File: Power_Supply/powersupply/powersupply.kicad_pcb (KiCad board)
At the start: 2 copper layers, 70.9 x 74.5 mm, 66 parts, among them J1 Conn_01x03, J2 USB_B_Micro, Q1 Q_PMOS_GDS, SW1 SW_Push, U1 AZ1117E-3.3, U10 MCP6001-OT, U2 ATSAMD10D13A-SS, U3 B0505S-2WR2, U4 TFT_OLED, U5 joystick-K1-1506DN-01, U6 MC33063AP1, U7 LM358P, U8 1x2, U9 1x2

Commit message: new layout
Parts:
- R11: renamed from R13; value 0.05 -> 0.1
- moved C2 1.33 mm to (68.3, 64.1)
- moved R1 0.44 mm to (66.5, 32.0)
- moved U3 0.35 mm to (53.2, 40.0)
- moved R104 0.34 mm to (89.0, 26.6)
- moved R105 0.28 mm to (86.0, 26.6)
- moved TP2 0.28 mm to (79.7, 51.4)
- moved L1 0.22 mm to (70.8, 77.3)
- renumbered R14 to R1, R9 to R10, R17 to R12, R6 to R13, R7 to R14, R10 to R15, R12 to R16, R11 to R17, R3 to R2, R2 to R3, R16 to R4, R15 to R5, R1 to R6, R4 to R7, R5 to R8, R8 to R9
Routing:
- net /SDA: track 18.1 -> 16.0 mm
- net /SCK: track 25.6 -> 24.2 mm
- net GND: track 44.3 -> 45.4 mm
- net Net-(C2-Pad1): track 5.84 -> 6.50 mm
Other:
- board size 70.9 x 74.5 mm -> 70.9 x 74.4 mm

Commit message: finalish changes
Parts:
- SW1: value SW_Push -> KMR2; footprint Button_Switch_THT:SW_PUSH_6mm -> Button_Switch_SMD:SW_Push_1P1T_NO_CK_KMR2
- TP10, TP11, TP8, TP9: footprint TestPoint:TestPoint_Pad_1.5x1.5mm -> powersupply:pads
- moved TP5 10.4 mm to (99.8, 73.6)
- moved SW1 3.61 mm to (112.6, 32.7), turned to 90 degrees
- moved TP8 3.58 mm to (76.4, 26.2)
- moved Q1 3.17 mm to (94.6, 74.7)
- moved TP10 2.91 mm to (79.8, 26.2)
- moved D2 2.83 mm to (90.0, 78.5)
- moved TP11 2.11 mm to (81.3, 26.2)
- moved TP9 1.89 mm to (77.8, 26.2)
- moved R11 1.84 mm to (89.4, 67.2)
- moved TP6 1.41 mm to (66.5, 47.1)
- moved R10 1.26 mm to (99.5, 63.4)
- moved R9 0.76 mm to (89.4, 59.8)
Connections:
- SW1 pad 1: Net-(R101-Pad2) -> GND
- SW1 pad 2: GND -> Net-(R101-Pad2)
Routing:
- net /Voltage_limit_divider: track 31.5 -> 41.1 mm
- net GND: track 45.4 -> 49.1 mm, vias 6 -> 8
- net Net-(R101-Pad2): track 48.0 -> 44.4 mm
- net /V_negative_out: track 61.8 -> 58.4 mm
- net /Boost_out: track 79.0 -> 76.8 mm
- net Net-(R10-Pad1): track 39.4 -> 37.6 mm
- net +3V3: track 121.5 -> 122.5 mm
- net /V_current_amplified: track 24.5 -> 25.3 mm
- net /V_boost_ctrl: track 69.5 -> 68.7 mm
- net Net-(D2-Pad1): track 15.6 -> 14.9 mm
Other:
- outline, holes or cut-outs redrawn
- board text removed: "- +"

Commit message: big CHANGES
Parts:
- removed R12, R5: 10k, Resistor_THT:R_Axial_DIN0207_L6.3mm_D2.5mm_P10.16mm_Horizontal
- removed R4: 100, Resistor_THT:R_Axial_DIN0207_L6.3mm_D2.5mm_P10.16mm_Horizontal
- added C6: .1uF, Capacitor_THT:C_Rect_L4.0mm_W2.5mm_P2.50mm, F.Cu at (92.6, 4.60)
- added D4: C503B 2.1V, LED_THT:LED_D3.0mm_Horizontal_O1.27mm_Z6.0mm, F.Cu at (86.8, 4.35)
- added R18: 300, Resistor_SMD:R_0805_2012Metric, F.Cu at (93.2, 8.10)
- added R19: 18.2k, Resistor_SMD:R_0805_2012Metric, F.Cu at (98.9, 4.05)
- added R20: 4.99k, Resistor_SMD:R_0805_2012Metric, F.Cu at (93.2, 11.1)
- C3: value 470u -> 470uF; footprint Capacitor_THT:CP_Radial_D10.0mm_P5.00mm -> Capacitor_THT:CP_Radial_D8.0mm_P3.50mm
- C4: value 470u -> 100uF; footprint Capacitor_THT:CP_Radial_D10.0mm_P5.00mm -> Capacitor_THT:CP_Radial_D6.3mm_P2.50mm
- C5: footprint Capacitor_THT:CP_Radial_D10.0mm_P5.00mm -> Capacitor_THT:CP_Radial_D6.3mm_P2.50mm
- D101: renamed from D3; footprint Diode_THT:D_DO-201AE_P15.24mm_Horizontal -> Diode_SMD:D_SOD-323
- J3: renamed from U9; footprint Connector_PinHeader_2.54mm:PinHeader_1x02_P2.54mm_Vertical -> Connector_PinHeader_2.54mm:PinHeader_1x02_P2.54mm_Horizontal
- L2: footprint Inductor_THT:L_Axial_L11.0mm_D4.5mm_P15.24mm_Horizontal_Fastron_MECC -> powersupply:11R102C_Inductor
- R1: value 1k -> 150
- R10, R13, R14, R15, R16, R17, R3, R6, R7, R8: footprint Resistor_THT:R_Axial_DIN0207_L6.3mm_D2.5mm_P10.16mm_Horizontal -> Resistor_SMD:R_0805_2012Metric
- R9: value 10k -> 130k; footprint Resistor_THT:R_Axial_DIN0207_L6.3mm_D2.5mm_P10.16mm_Horizontal -> Resistor_SMD:R_0805_2012Metric
- TP10: value TestPoint -> pin_2_pad
- TP11: value TestPoint -> pin_2_alt
- TP8: value TestPoint -> pin_1_alt
- TP9: value TestPoint -> pin_1_pad
- U10: value MCP6001-OT -> INA199; footprint Package_TO_SOT_SMD:SOT-23-5 -> Package_TO_SOT_SMD:SOT-363_SC-70-6
- U6: footprint Package_SO:SOIC-8_3.9x4.9mm_P1.27mm -> Package_DIP:DIP-8_W7.62mm
- moved TP4 109.9 mm to (2.20, 103.4)
- moved TP3 105.0 mm to (-0.90, 87.7)
- moved TP5 89.9 mm to (12.7, 95.9)
- moved TP6 70.6 mm to (2.30, 76.3)
- moved TP1 67.9 mm to (13.9, 81.5)
- moved TP7 47.7 mm to (13.8, 110.9)
- moved U10 47.4 mm to (97.6, 8.55), turned to 0 degrees
- moved L1 27.2 mm to (43.8, 80.8)
- moved J3 26.8 mm to (78.2, 87.7)
- moved R3 22.0 mm to (42.5, 72.9), turned to 90 degrees
- moved R2 20.4 mm to (39.2, 79.0)
- moved L2 20.4 mm to (33.4, 68.1)
- moved U3 17.9 mm to (36.0, 44.9)
- moved D101 17.4 mm to (46.5, 37.7)
- moved C105 17.3 mm to (54.8, 39.3)
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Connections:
- C105 pad 1: /V_boost_ctrl -> /V_lin_ctrl
- R103 pad 1: /V_boost_ctrl -> /V_lin_ctrl
- U10 pad 1: /V_current_amplified -> GND
- U10 pad 3: Net-(R10-Pad1) -> +3V3
- U10 pad 4: Net-(R4-Pad1) -> /V_negative_out
- U10 pad 5: +3V3 -> GND
- U2 pad 18: /V_lin_ctrl -> /V_boost_ctrl
- U2 pad 8: /V_positive_out -> Net-(R19-Pad2)
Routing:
- net /V_positive_out: track 151.8 -> 0.00 mm
- net +3V3: track 122.5 -> 0.00 mm
- net +5V: track 81.1 -> 0.00 mm, vias 2 -> 0
- net /Boost_out: track 76.8 -> 0.00 mm
- net /V_boost_ctrl: track 68.7 -> 0.00 mm
- net Net-(C3-Pad1): track 62.7 -> 0.00 mm
- net /V_lin_ctrl: track 61.2 -> 0.00 mm
- net /V_negative_out: track 58.4 -> 0.00 mm, vias 2 -> 0
- net /V_curr_lim: track 57.8 -> 0.00 mm, vias 2 -> 0
- net GND: track 49.1 -> 0.00 mm, vias 8 -> 1
- net Net-(R101-Pad2): track 44.4 -> 0.00 mm, vias 2 -> 0
- net /Voltage_limit_divider: track 41.1 -> 0.00 mm
- net Net-(R10-Pad1): track 37.6 -> 0.00 mm
- net /Current_limit_divider: track 30.4 -> 0.00 mm
- net Net-(D2-Pad2): track 29.0 -> 0.00 mm
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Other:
- outline, holes or cut-outs redrawn

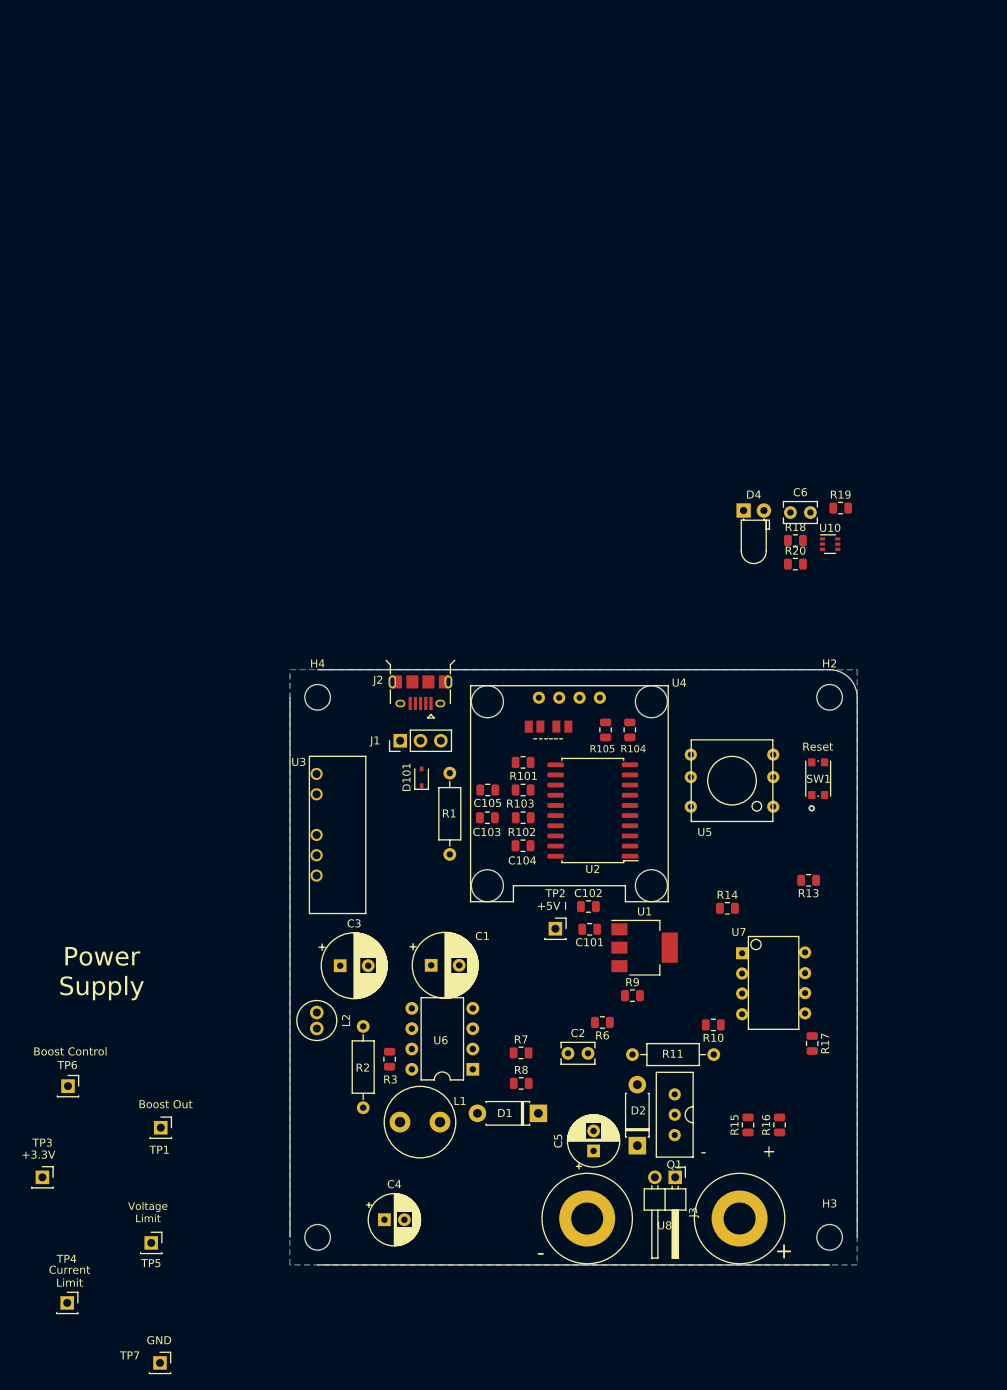
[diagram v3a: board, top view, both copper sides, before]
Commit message: new layout for power supply
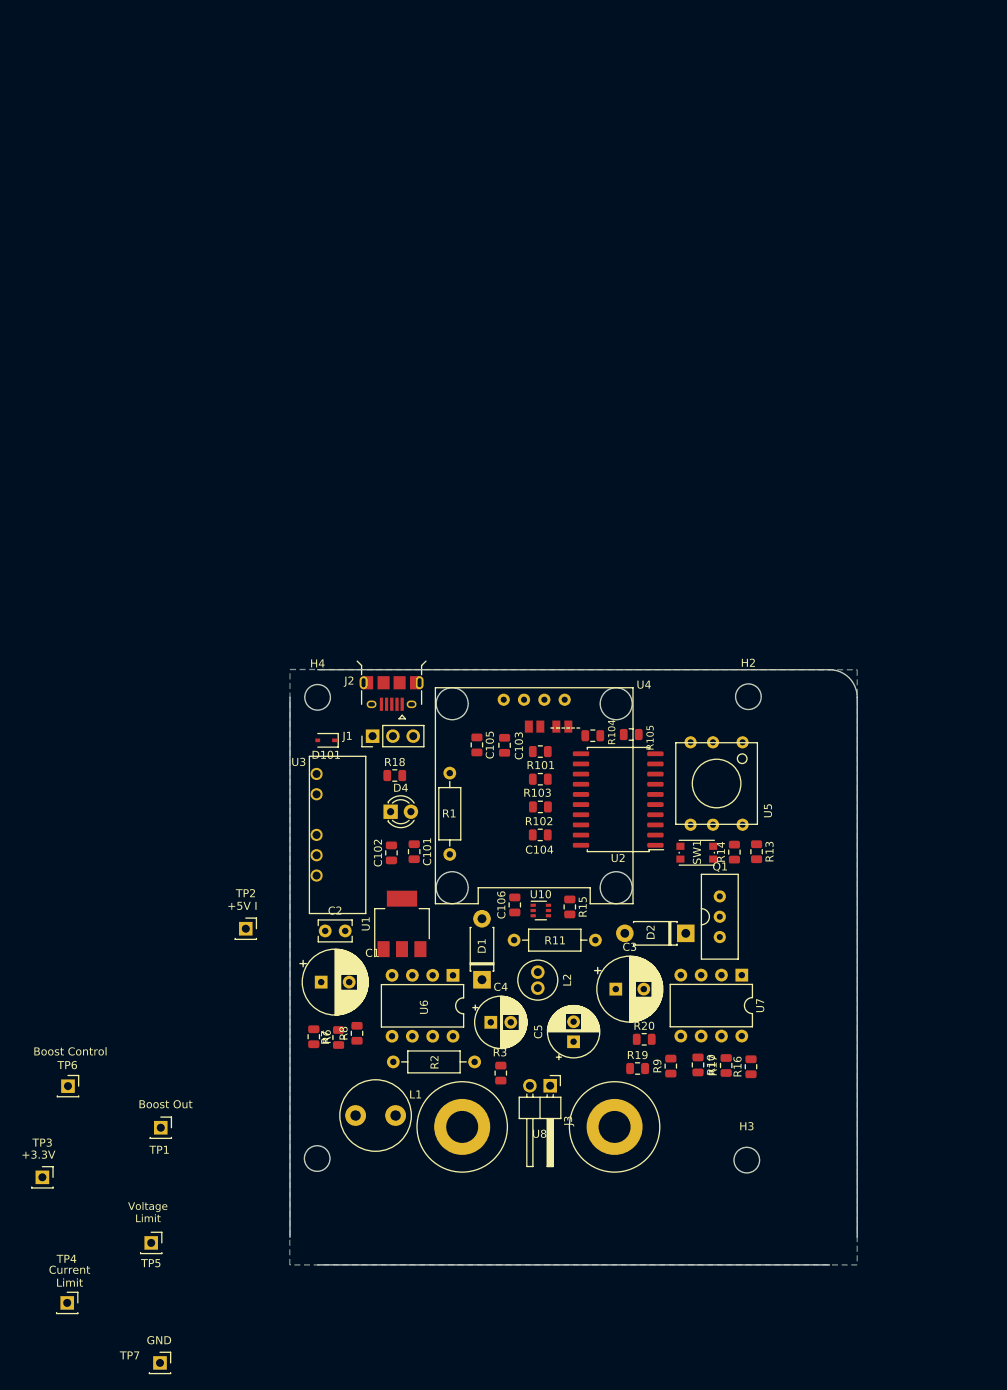
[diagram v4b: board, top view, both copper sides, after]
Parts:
- removed C6: .1uF, Capacitor_THT:C_Rect_L4.0mm_W2.5mm_P2.50mm
- added C106: .1uF, Capacitor_SMD:C_0805_2012Metric, F.Cu at (58.1, 53.6)
- D4: footprint LED_THT:LED_D3.0mm_Horizontal_O1.27mm_Z6.0mm -> LED_THT:LED_D3.0mm
- U7: footprint powersupply:LM358P -> Package_DIP:DIP-8_W7.62mm
- moved R19 74.5 mm to (73.5, 74.1)
- moved R20 62.3 mm to (74.3, 70.5)
- moved U10 58.4 mm to (61.4, 54.4)
- moved R18 58.1 mm to (43.1, 37.5)
- moved D4 58.0 mm to (42.6, 42.0)
- moved TP2 38.7 mm to (24.5, 56.6)
- moved R6 36.1 mm to (33.0, 70.1), turned to 270 degrees
- moved R15 35.2 mm to (65.0, 53.9), turned to 270 degrees
- moved C3 34.6 mm to (70.8, 64.2)
- moved C2 34.0 mm to (34.5, 56.9)
- moved U1 30.5 mm to (44.0, 56.0), turned to 90 degrees
- moved L2 28.1 mm to (61.0, 63.0)
- moved C4 28.0 mm to (55.1, 68.3)
- moved D2 27.2 mm to (79.5, 57.2), turned to 180 degrees
- moved C102 25.5 mm to (42.7, 47.1), turned to 90 degrees
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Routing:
- net GND: vias 1 -> 0
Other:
- board text removed: "+"
- board text removed: "-"
- board text removed: "Power Supply"
- board text removed: "Reset"

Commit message: big CHANGES
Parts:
- R1: footprint Resistor_THT:R_Axial_DIN0207_L6.3mm_D2.5mm_P10.16mm_Horizontal -> Resistor_SMD:R_0805_2012Metric
- R18: footprint Resistor_SMD:R_0805_2012Metric -> Resistor_THT:R_Axial_DIN0207_L6.3mm_D2.5mm_P10.16mm_Horizontal
- moved SW1 40.2 mm to (43.2, 33.0), turned to 0 degrees
- moved R11 34.4 mm to (41.5, 79.7)
- moved R20 23.5 mm to (84.3, 49.1), turned to 180 degrees
- moved R19 22.9 mm to (84.2, 53.9)
- moved R2 21.6 mm to (31.6, 75.3), turned to 0 degrees
- moved L1 19.5 mm to (54.4, 69.0)
- moved C4 19.1 mm to (70.5, 57.1), turned to 180 degrees
- moved D2 17.5 mm to (74.1, 73.8), turned to 0 degrees
- moved R10 16.9 mm to (68.1, 62.8), turned to 0 degrees
- moved R1 16.8 mm to (33.2, 37.0)
- moved C2 15.6 mm to (49.9, 59.2), turned to 90 degrees
- moved C3 14.4 mm to (58.5, 56.6)
- moved R9 12.8 mm to (68.1, 65.3), turned to 180 degrees
- moved R13 12.2 mm to (76.5, 49.7), turned to 180 degrees
- moved R3 11.5 mm to (44.9, 75.6), turned to 90 degrees
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
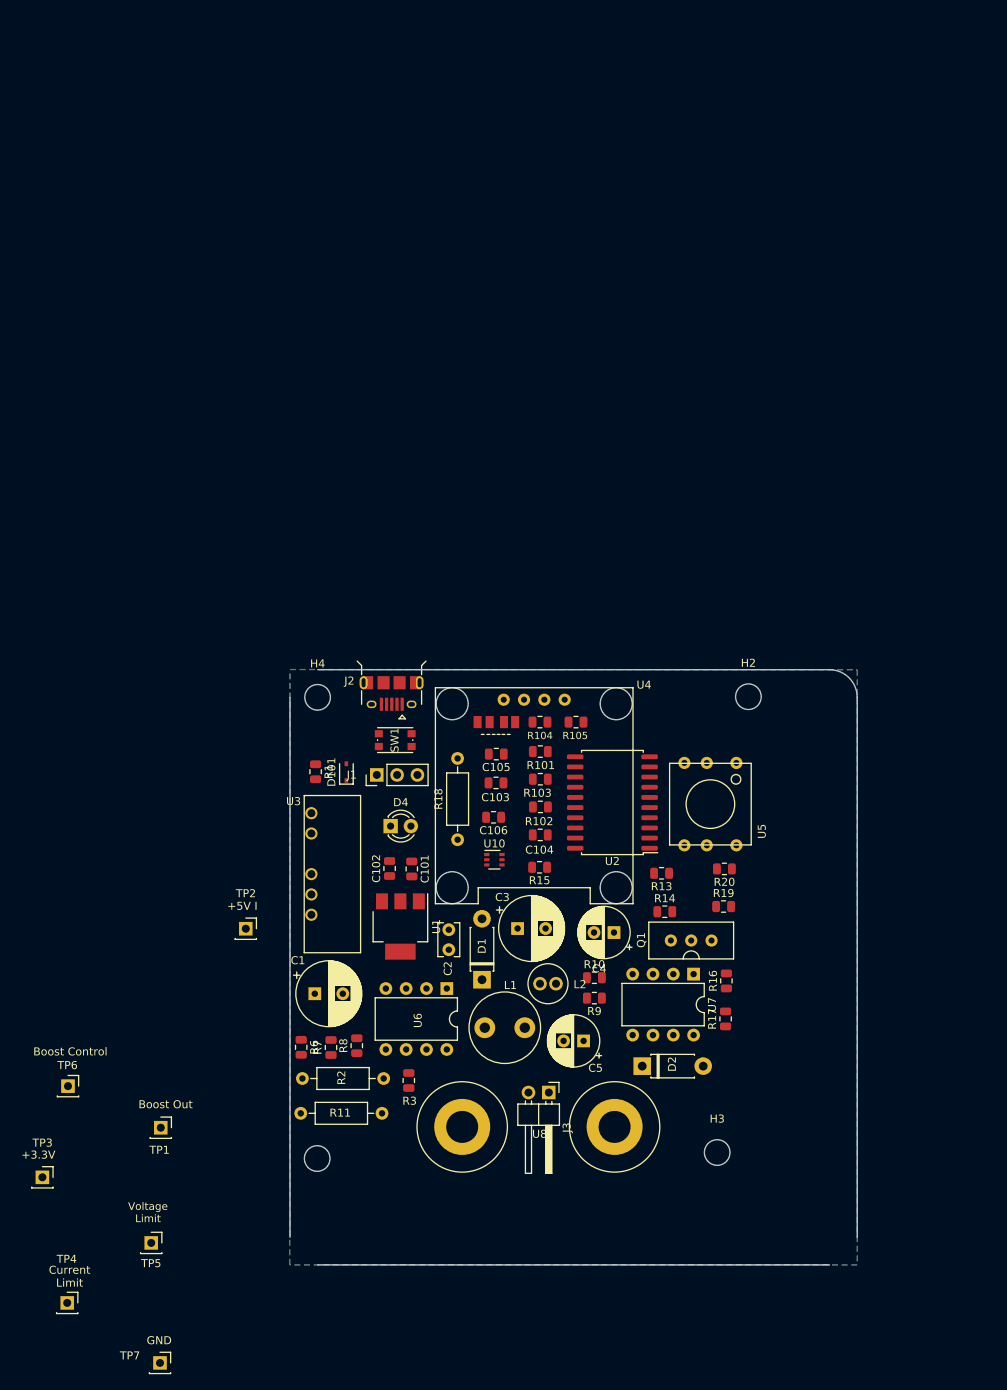
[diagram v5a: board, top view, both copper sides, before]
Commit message: new layout with SMD components
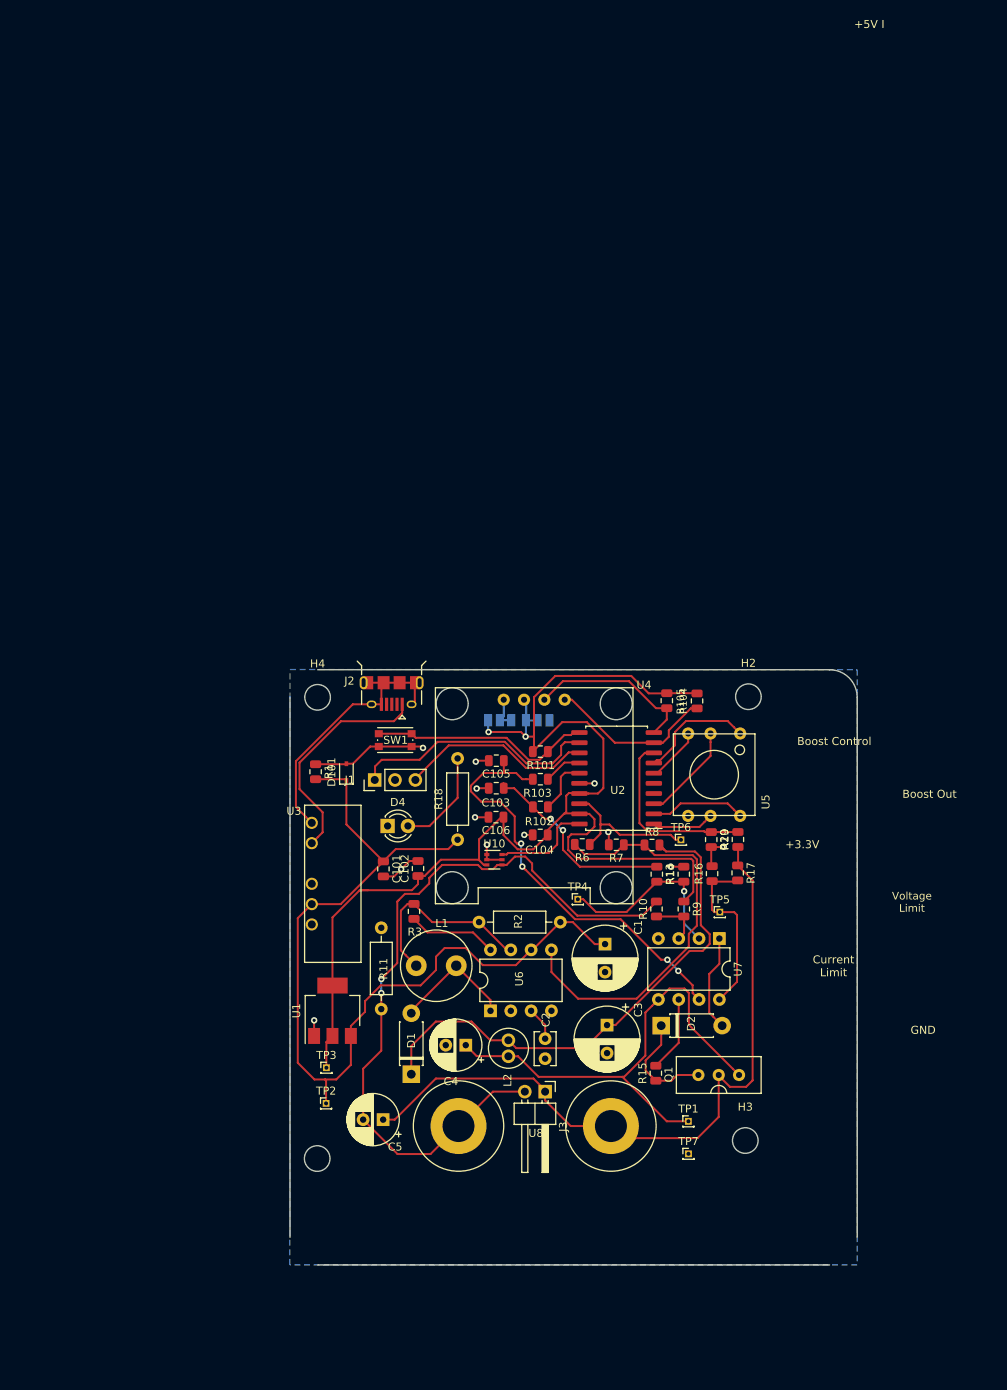
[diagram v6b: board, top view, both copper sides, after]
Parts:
- added TP12: Pad1_default, powersupply:pads, B.Cu at (57.7, 30.6)
- added TP13: TestPoint, powersupply:pads, B.Cu at (59.5, 30.6)
- R18: value 300 -> 560
- TP1, TP2, TP3, TP4, TP5, TP6, TP7: footprint Connector_PinSocket_2.54mm:PinSocket_1x01_P2.54mm_Vertical -> Connector_PinHeader_1.00mm:PinHeader_1x01_P1.00mm_Vertical
- TP10, TP11, TP8, TP9: moved to B.Cu
- moved TP6 82.6 mm to (78.9, 45.5)
- moved TP5 82.2 mm to (83.8, 54.5)
- moved TP4 81.4 mm to (66.0, 52.9)
- moved TP7 71.0 mm to (79.9, 84.8)
- moved TP1 66.0 mm to (79.8, 80.7)
- moved R8 44.6 mm to (75.3, 46.2), turned to 0 degrees
- moved R7 43.7 mm to (70.8, 46.1), turned to 180 degrees
- moved R6 43.3 mm to (66.6, 46.1), turned to 180 degrees
- moved TP3 38.1 mm to (34.6, 74.0)
- moved C1 36.8 mm to (69.4, 58.5), turned to 270 degrees
- moved R15 29.6 mm to (75.8, 74.7), turned to 90 degrees
- moved R2 29.5 mm to (53.7, 55.8)
- moved C5 26.9 mm to (41.7, 80.5)
- moved TP2 24.0 mm to (34.6, 78.5)
- moved C4 23.3 mm to (52.0, 71.2)
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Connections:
- U2 pad 1: /center -> /right
- U2 pad 2: /up -> /center
- U2 pad 7: /right -> /up
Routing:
- net +3V3: track 0.00 -> 161.1 mm, vias 0 -> 2
- net +5V: track 0.00 -> 116.3 mm
- net /V_negative_out: track 0.00 -> 94.1 mm, vias 0 -> 2
- net /V_positive_out: track 0.00 -> 89.7 mm
- net Net-(C3-Pad1): track 0.00 -> 66.9 mm
- net /Boost_out: track 0.00 -> 61.3 mm
- net /V_lin_ctrl: track 0.00 -> 54.3 mm, vias 0 -> 4
- net Net-(R6-Pad2): track 0.00 -> 52.2 mm
- net GND: track 0.00 -> 45.4 mm, vias 0 -> 12
- net Net-(J2-Pad5): track 0.00 -> 33.6 mm
- net /SWCLK: track 0.00 -> 30.1 mm
- net Net-(J2-Pad1): track 0.00 -> 28.3 mm
- net Net-(R101-Pad2): track 0.00 -> 27.2 mm
- net /V_curr_lim: track 0.00 -> 25.8 mm, vias 0 -> 2
- net Net-(R19-Pad2): track 0.00 -> 25.4 mm
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
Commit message: finished layout
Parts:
- removed U4: TFT_OLED, powersupply:TFT_OLED_display
- added MOD1: TFT_OLED, powersupply:TFT_OLED_display, F.Cu at (59.3, 43.9)
- moved H3 4.92 mm to (86.1, 88.0)
- moved TP7 4.34 mm to (77.8, 88.6)
- moved TP1 4.33 mm to (77.8, 84.5)
- moved D1 4.33 mm to (43.9, 79.0)
- moved R17 4.15 mm to (84.8, 53.6)
- moved R16 4.11 mm to (81.4, 53.6)
- moved H2 4.10 mm to (86.1, 31.5)
- moved D2 4.04 mm to (75.2, 72.6)
- moved L2 4.04 mm to (56.1, 75.4)
- moved Q1 4.04 mm to (82.4, 78.8)
- moved R15 4.04 mm to (74.5, 78.5)
- moved TP2 4.04 mm to (33.3, 82.3)
- moved C5 4.04 mm to (40.5, 84.3)
- moved J3 4.04 mm to (60.7, 80.8)
- moved U1 4.04 mm to (34.1, 70.7)
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- renumbered U8 to J4
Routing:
- net /Boost_out: track 61.3 -> 60.5 mm
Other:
- board size 70.9 x 74.4 mm -> 60.8 x 63.3 mm
- board text added: "+5V"
- board text added: "Boost"
- board text added: "V Limit"
- board text removed: "Boost Control"
- board text removed: "Voltage Limit"

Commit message: small changes
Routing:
- net /V_positive_out: track 89.7 -> 90.4 mm
- net Net-(D2-Pad1): track 13.8 -> 14.6 mm
- net +5V: track 116.3 -> 116.8 mm
